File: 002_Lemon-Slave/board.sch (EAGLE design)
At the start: 61 parts, among them IC1 74HC595N, IC2 74HC595N, IC3 74HC595N, IC4 7805TV, U1 ATTINY85-20P, X1 MKDSN1,5/2-5,08, X2 MKDSN1,5/2-5,08, X3 MKDSN1,5/2-5,08

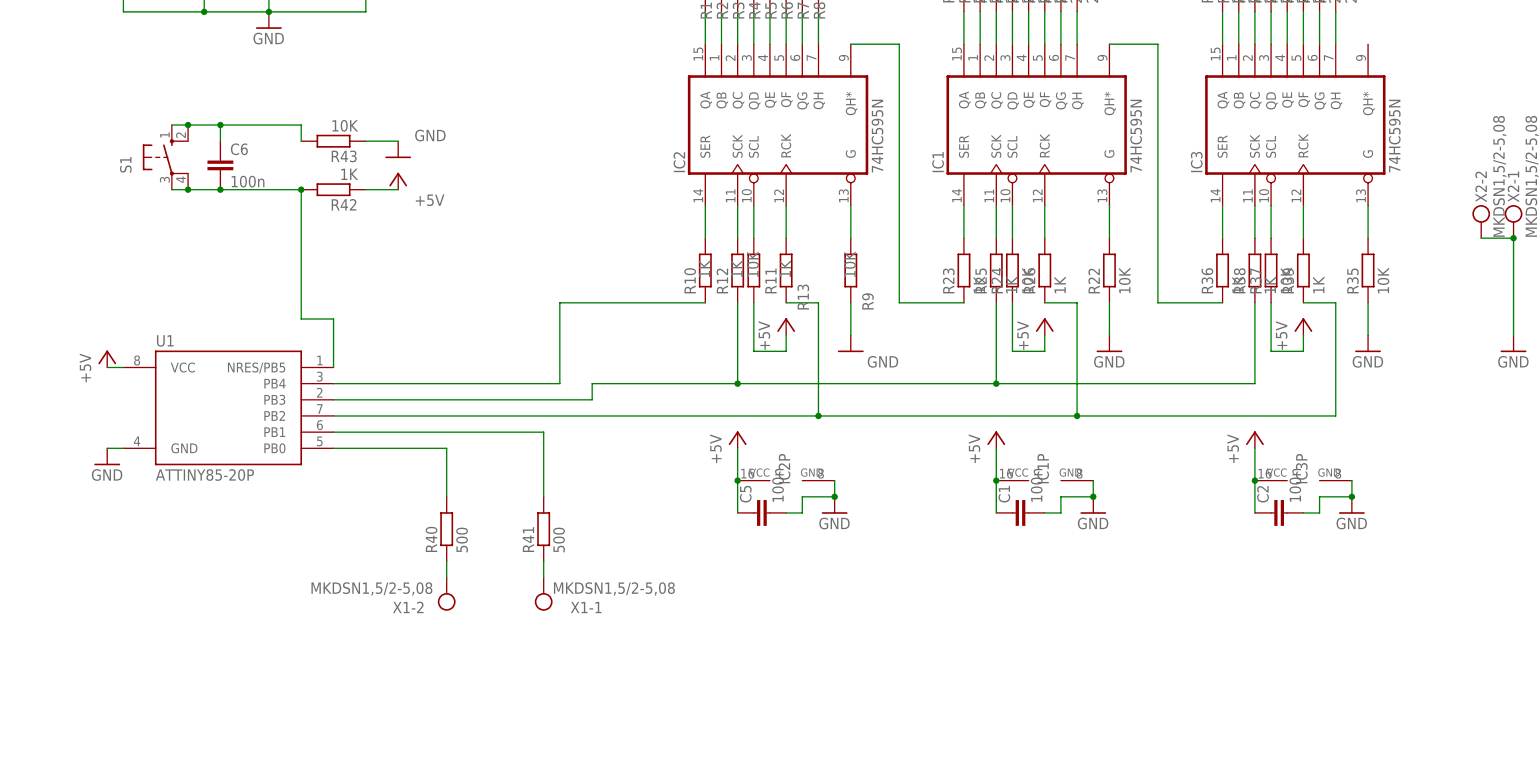
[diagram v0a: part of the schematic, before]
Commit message: fixed error in lemon-light slave controller
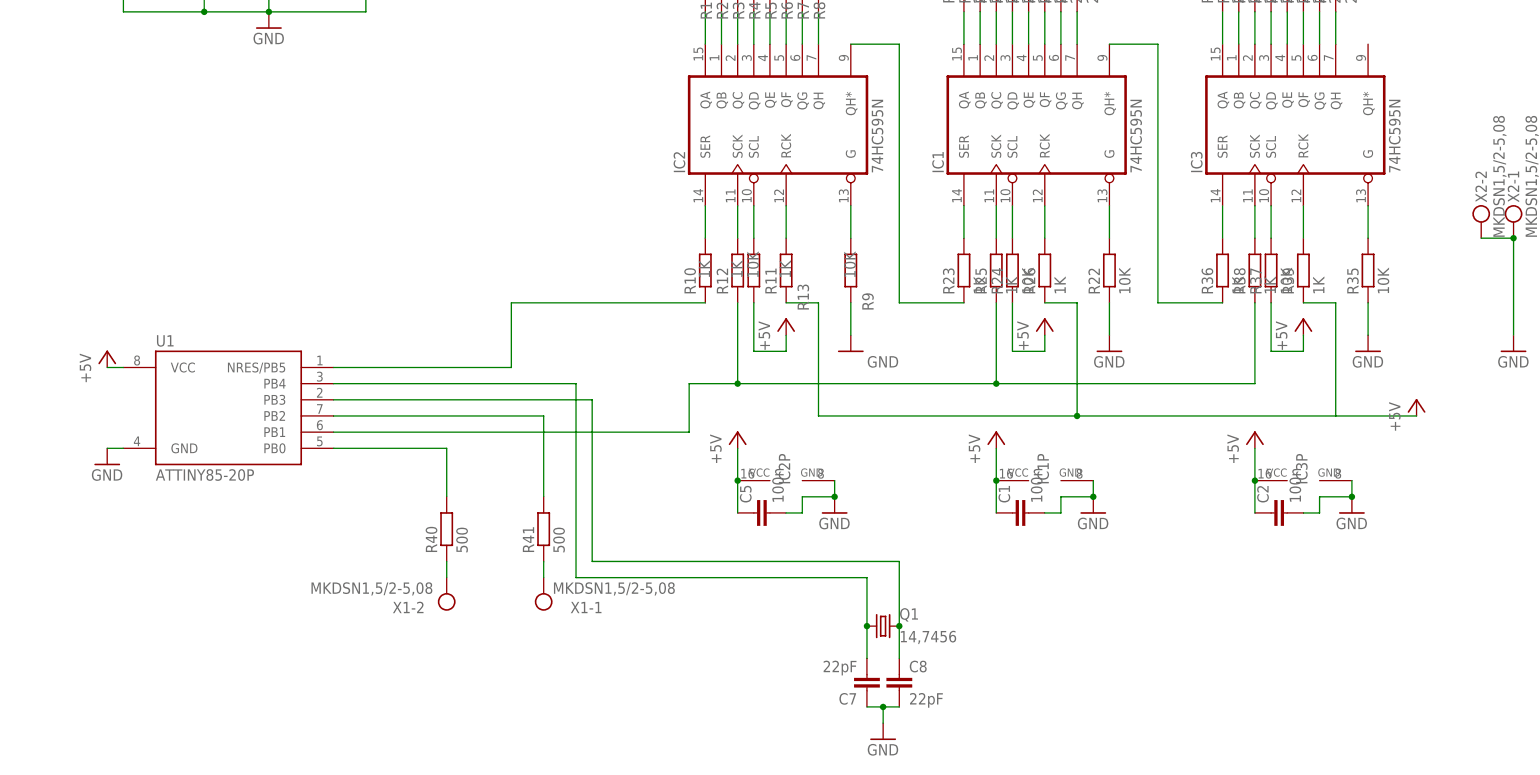
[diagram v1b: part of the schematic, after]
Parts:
- removed C6: 100n, capacitor-wima:C5/3
- removed R42: 1K, resistor:R-EU_0207/10
- removed R43: 10K, resistor:R-EU_0207/10
- removed S1: (no value), switch-omron:10-XX
- added C7, C8: 22pF, resistor:C-EU025-025X050
- added Q1: 14,7456, crystal:CRYSTALHC49S
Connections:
- removed net N$68: R13.1, R26.1, R39.1, U1.PB2
- removed net N$75: C6.2, R42.2, S1.P, S1.P1, U1.NRES/PB5
- new net N$78: C8.1, Q1.2, U1.PB3
- net +5V: now also R13.1, R26.1, R39.1; no longer R42.1
- net GND: now also C7.1, C8.2; no longer R43.1
- net N$67: now also U1.PB1; no longer U1.PB3
- net N$70: now also U1.PB2; no longer U1.PB1
- net N$73: now also U1.NRES/PB5; no longer U1.PB4
- net N$74: now also C7.2, Q1.1, U1.PB4; no longer C6.1, R43.2, S1.S, S1.S1

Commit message: update lemon light main controller
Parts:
- removed U1: ATTINY85-20P, attiny25_45_85:ATTINY85-20P
- added C6: 4,7nF, rcl:C-EUC0805K
- added JP4: (no value), pinhead:PINHD-1X3
- added R42: 1K, resistor:R-EU_M0805
- added R43: 10K, resistor:R-EU_M0805
- added S1: (no value), switch-omron:10-XX
- added U$1: ATTINY406, My_AVRs:ATTINY406
- C1, C2, C3, C4, C5: device capacitor-wima:C5/3 -> rcl:C-EUC0805K
- C7, C8: value 22pF -> 12pF; device resistor:C-EU025-025X050 -> rcl:C-EUC0805K
- IC1, IC2, IC3: value 74HC595N -> 74HC595D; device 74xx-eu:74HC595N -> 74xx-eu:74HC595D
- Q1: device crystal:CRYSTALHC49S -> crystal:CRYSTALSM49
- R1, R10, R11, R12, R13, R14, R15, R16, R17, R18, R19, R2, R20, R21, R22, R23, R24, R25, R26, R27, R28, R29, R3, R30, R31, R32, R33, R34, R35, R36, R37, R38, R39, R4, R5, R6, R7, R8, R9: device resistor:R-EU_0207/10 -> resistor:R-EU_M0805
- R40, R41: value 500 -> 100; device resistor:R-EU_0207/10 -> resistor:R-EU_M0805
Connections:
- new net N$68: R13.1, R26.1, R39.1, U$1.PC0
- new net N$75: C6.1, JP4.2, R43.2, S1.S, S1.S1, U$1.PA0
- new net N$76: C6.2, R42.2, S1.P, S1.P1
- net +5V: now also JP4.1, R43.1, U$1.VDD; no longer R13.1, R26.1, R39.1, U1.VCC
- net GND: now also JP4.3, R42.1, U$1.GND; no longer U1.GND
- net N$67: now also U$1.PC1; no longer U1.PB1
- net N$69: now also U$1.PB3; no longer U1.PB0
- net N$70: now also U$1.PB2; no longer U1.PB2
- net N$73: now also U$1.PC2; no longer U1.NRES/PB5
- net N$74: now also U$1.PA3; no longer U1.PB4
- net N$78: now also U$1.PB5; no longer U1.PB3
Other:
- note added: "Common-ground for the LEDs"
- note added: "External Crystal: Stabilize the working frequency of the AVR to be able to use the internal UART interface"
- note added: "Power Supply: - 8V Input, 5V output - capacitors for stability"
- note added: "Shift Registers: - driving the LEDs - between every LED and the shift register a resistor is placed - the shift registers are driven by the AVR"
- note added: "UART breakout connected to screw terminal"
- note added: "programming breakout"
- note added: "reset circuit"
- moved on the sheet: C1, C2, C3, C4, C5, C7, C8, IC1, IC1P, IC2, IC2P, IC3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
